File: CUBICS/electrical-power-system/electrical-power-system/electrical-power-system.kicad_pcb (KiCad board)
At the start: 2 copper layers, 90.2 x 95.9 mm, 134 parts, among them IC1 TPS630701RNMT, IC2 TPS630701RNMT, J1 Conn_01x02, J10 Conn_02x26_Odd_Even, J11 Conn_01x05_Pin, J12 Conn_02x26_Odd_Even, J13 Conn_01x03_Pin, J14 AVR-ISP-6, J2 Conn_01x02, J3 Conn_01x02, J4 Conn_01x02, J5 Conn_01x02, J6 Conn_01x02, J7 Conn_01x05_Pin, J8 Conn_01x05_Pin, J9 Conn_01x05_Pin, Q1 NMOS, Q10 CSD16406Q3, Q2 PMOS, Q3 CSD16406Q3, Q4 CSD16406Q3, Q5 CSD16406Q3, Q6 CSD16406Q3, Q7 CSD16406Q3, Q8 CSD16406Q3, Q9 CSD16406Q3, SW1 SW_Push_SPDT, SW2 SW_Push_SPDT, SW3 SW_Push_SPDT, SW4 SW_Push_SPDT, SW5 SW_Push_SPDT, SW6 SW_Push_SPDT, SW7 SW_Push_SPDT, U1 LTC4054XES5-4.2, U10 BQ297xy, U2 INA180, U3 INA180, U4 LT1762-3.3, U5 ATmega328-P, U6 TCAN1043xDxQ1, U7 BQ297xy, U8 BQ297xy, U9 BQ297xy

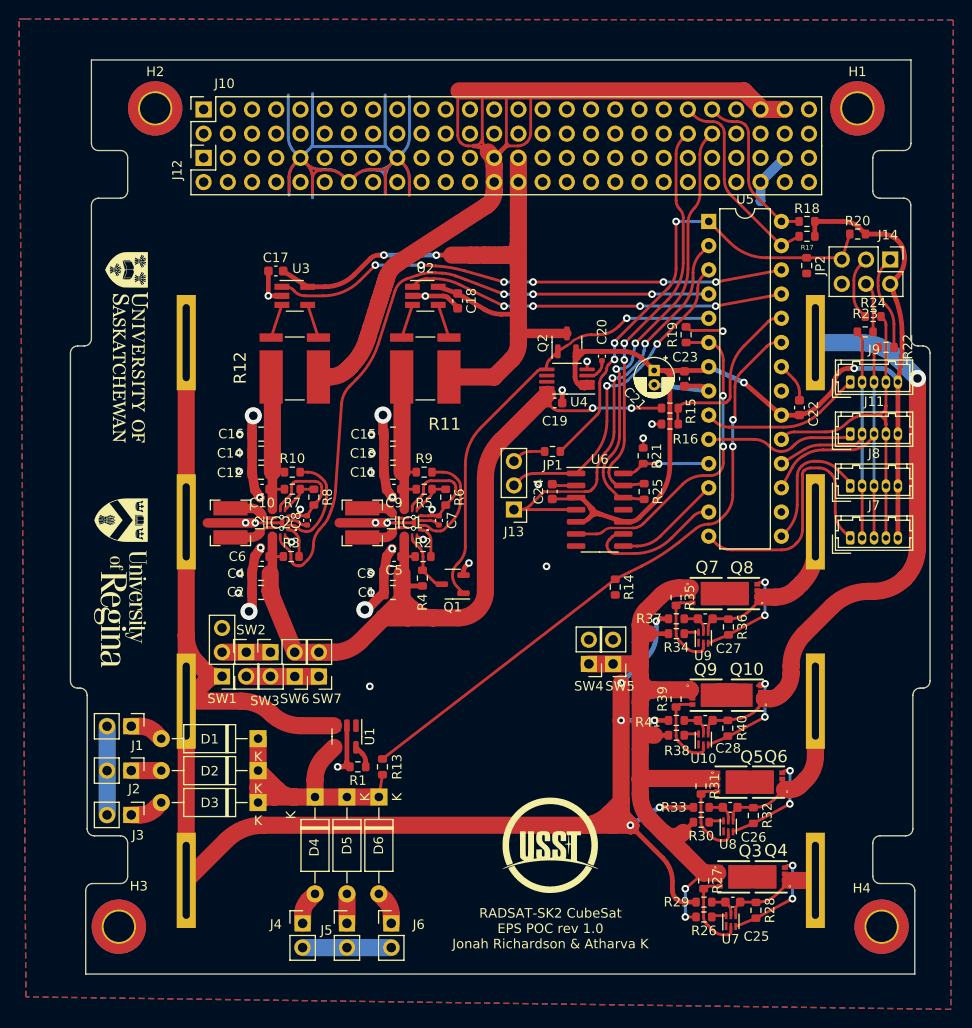
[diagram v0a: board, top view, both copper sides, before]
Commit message: Added thermal relief pads to ground plane
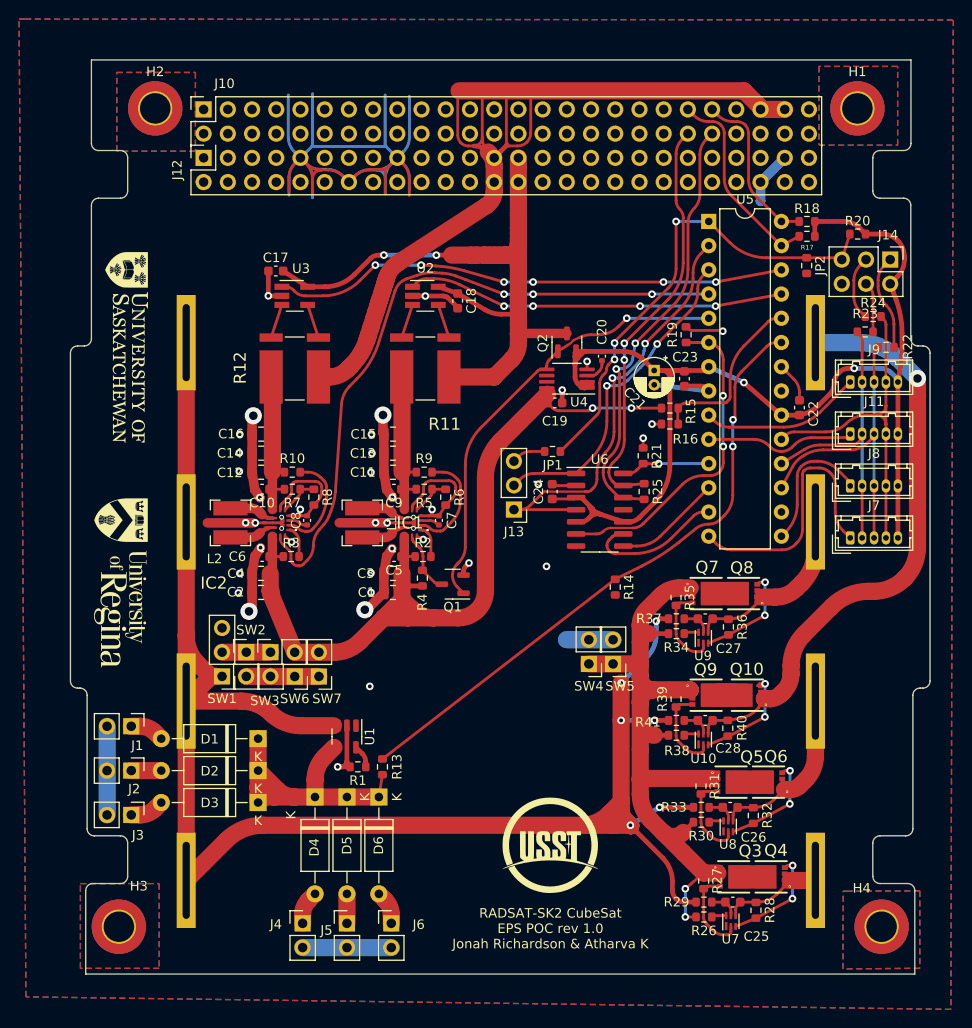
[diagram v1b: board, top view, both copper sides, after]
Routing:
- net GND: track 242.5 -> 247.4 mm
- net Net-(IC2-L1): track 4.92 -> 6.15 mm
- net Net-(IC1-L2): track 4.07 -> 5.27 mm
- net Net-(IC1-L1): track 4.99 -> 6.18 mm
- net Net-(IC2-L2): track 4.64 -> 5.62 mm
